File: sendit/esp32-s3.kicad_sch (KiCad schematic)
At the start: 47 parts, among them J9 USB_TYPE_C_16PIN, Q1 FDC6330L, Q2 S8050, Q3 S8050, SW1 RESET, SW2 BOOT, U1 ESP32-S3-WROOM-1-N16R8, U2 USBLC6-2SC6, U3 XC6210B332MR, U4 CH334F, U5 CH343P, Y1 12Mhz, Y2 32.768kHz

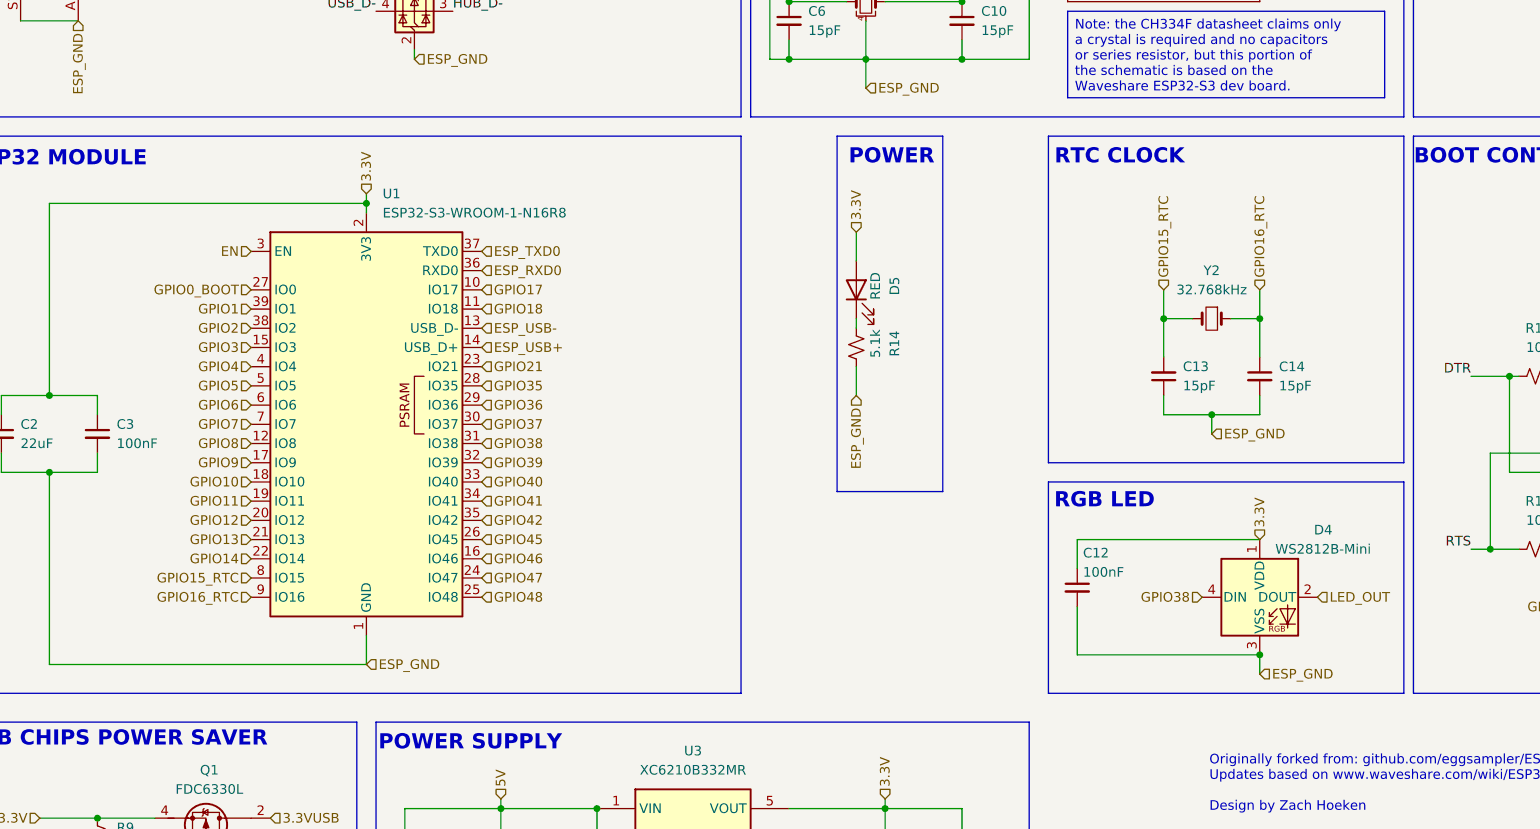
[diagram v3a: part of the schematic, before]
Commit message: started work on the rev c schematic
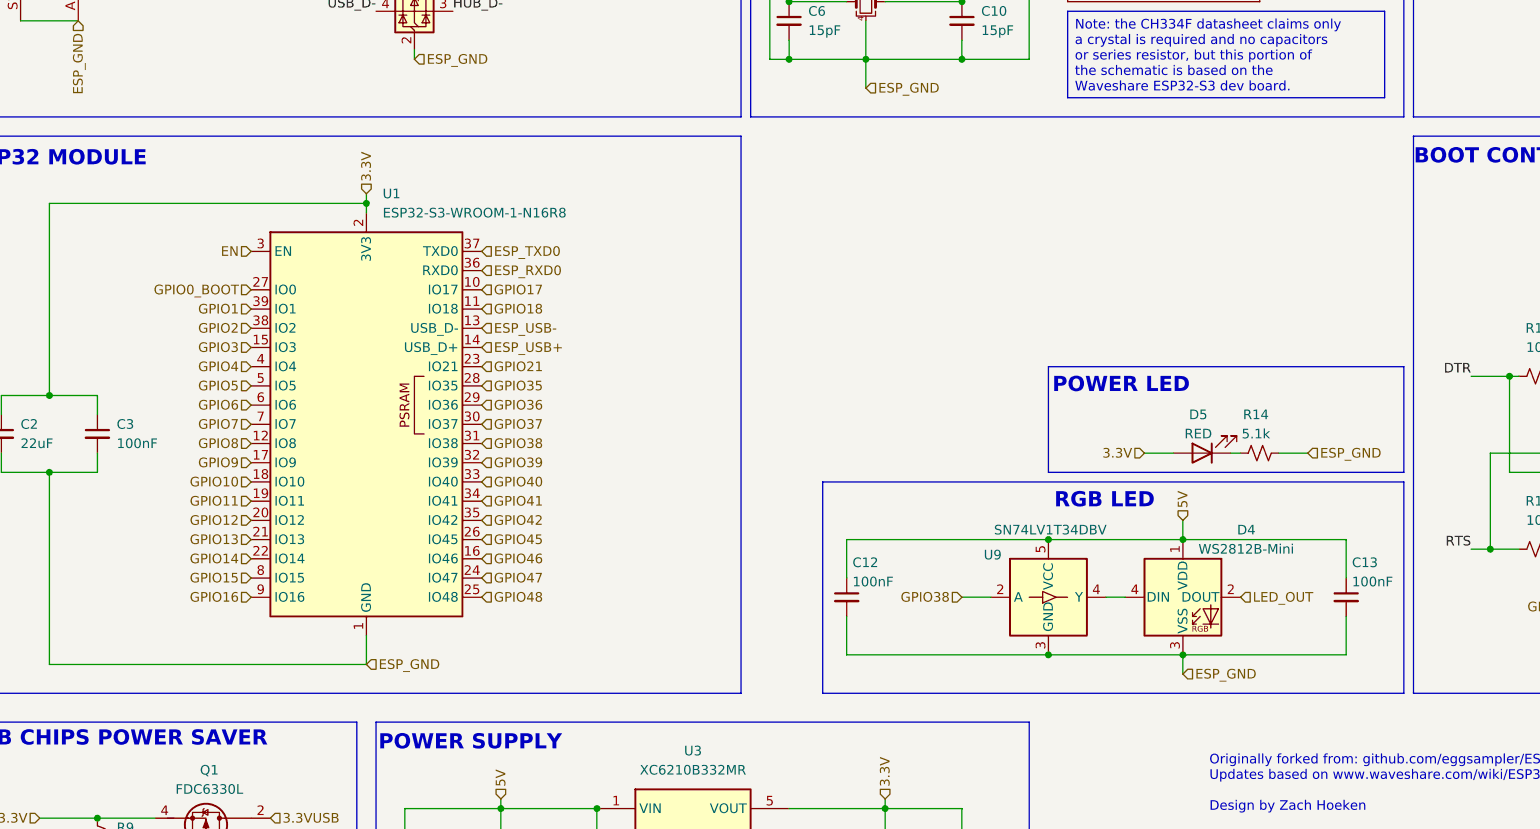
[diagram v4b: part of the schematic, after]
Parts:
- removed C14: 15pF, Capacitor_SMD:C_0603_1608Metric, symbol Device:C_Small
- removed Y2: 32.768kHz, Crystal:Crystal_SMD_3215-2Pin_3.2x1.5mm, symbol Device:Crystal_Small
- added U9: SN74LV1T34DBV, Package_TO_SOT_SMD:SOT-23-5, symbol Logic_LevelTranslator:SN74LV1T34DBV
- C13: value 15pF -> 100nF
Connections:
- net 3.3V: no longer C12.1, D4.1 (VDD)
- net 5V: now also C12.1, C13.1, D4.1 (VDD), U9.5 (VCC)
- net ESP_GND: now also C13.2, U9.3 (GND); no longer C13.1
- net GPIO38: now also U9.2 (A); no longer D4.4 (DIN)
- net GPIO15_RTC renamed GPIO15
- net GPIO15: no longer C13.2
- net GPIO16_RTC renamed GPIO16
- new net: D4.4 (DIN), U9.4 (Y)
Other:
- note added: "POWER LED"
- note removed: "POWER"
- note removed: "RTC CLOCK"
- moved on the sheet: C12, D4, D5, R14

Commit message: more work on rev c board schematic
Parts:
- added TP20: ~, TestPoint:TestPoint_THTPad_D2.0mm_Drill1.0mm, symbol Connector:TestPoint
- D5: value RED -> GREEN
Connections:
- net 3.3V: now also TP20.1
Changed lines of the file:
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@@
 	)
 	(junction
+		(at 72.39 175.26)
+		(diameter 0)
+		(color 0 0 0 0)
+	)
+	(junction
 		(at 31.75 176.53)
 		(diameter 0)
@@
 	)
 	(junction
+		(at 146.05 175.26)
+		(diameter 0)
+		(color 0 0 0 0)
+	)
+	(junction
 		(at 229.87 35.56)
 		(diameter 0)
@@
 	(wire
 		(pts
-			(xy 85.09 173.99) (xy 85.09 175.26)
+			(xy 72.39 173.99) (xy 72.39 175.26)
 		)
 		(stroke
@@
 	(wire
 		(pts
+			(xy 72.39 175.26) (xy 85.09 175.26)
+		)
+		(stroke
+			(width 0)
+			(type default)
+		)
+	)
+	(wire
+		(pts
 			(xy 144.78 26.67) (xy 144.78 27.94)
 		)
@@
 	(wire
 		(pts
-			(xy 135.89 173.99) (xy 135.89 175.26)
+			(xy 146.05 173.99) (xy 146.05 175.26)
 		)
 		(stroke
@@
 	(wire
 		(pts
-			(xy 85.09 175.26) (xy 72.39 175.26)
-		)
-		(stroke
-			(width 0)
-			(type default)
-		)
-	)
-	(wire
-		(pts
 			(xy 218.44 45.72) (xy 228.6 45.72)
 		)
@@
 	(hierarchical_label "5V"
 		(shape input)
-		(at 85.09 173.99 90)
+		(at 72.39 173.99 90)
 		(effects
 			(font
@@
 	(hierarchical_label "3.3V"
 		(shape input)
-		(at 135.89 173.99 90)
+		(at 146.05 173.99 90)
 		(effects
 			(font
@@
 			)
 		)
-		(property "Value" "RED"
+		(property "Value" "GREEN"
 			(at 177.292 125.73 0)
 			(effects
@@
 					(unit 1)
 				)
+			)
+		)
+	)
+	(symbol
+		(lib_id "Connector:TestPoint")
+		(at 135.89 175.26 0)
+		(unit 1)
+		(exclude_from_sim no)
+		(in_bom no)
+		(on_board yes)
+		(dnp no)
+		(property "Reference" "TP20"
+			(at 134.366 170.18 0)
+			(effects
+				(font
+					(size 1.27 1.27)
+				)
+				(justify left)
+			)
+		)
+		(property "Value" "~"
+			(at 138.43 173.2279 0)
+			(effects
+				(font
+					(size 1.27 1.27)
+				)
+				(justify left)
+				(hide yes)
+			)
+		)
+		(property "Footprint" "TestPoint:TestPoint_THTPad_D2.0mm_Drill1.0mm"
+			(at 140.97 175.26 0)
+			(effects
+				(font
+					(size 1.27 1.27)
+				)
+				(hide yes)
+			)
+		)
+		(property "Datasheet" "~"
+			(at 140.97 175.26 0)
+			(effects
+				(font
+					(size 1.27 1.27)
+				)
+				(hide yes)
+			)
+		)
+		(property "Description" "test point"
+			(at 135.89 175.26 0)
+			(effects
+				(font
+					(size 1.27 1.27)
+				)
+				(hide yes)
+			)
+		)
+		(property "LCSC Part Name" ""
+			(at 135.89 175.26 0)
+			(effects
+				(font
+					(size 1.27 1.27)
+				)
+				(hide yes)
+			)
+		)
+		(property "Manufacturer" ""
+			(at 135.89 175.26 0)
+			(effects
+				(font
+					(size 1.27 1.27)
+				)
+				(hide yes)
+			)
+		)
+		(property "Manufacturer Part" ""
+			(at 135.89 175.26 0)
+			(effects
+				(font
+					(size 1.27 1.27)
+				)
+				(hide yes)
+			)
+		)
+		(property "Supplier" ""
+			(at 135.89 175.26 0)
+			(effects
+				(font
+					(size 1.27 1.27)
+				)
+				(hide yes)
+			)
+		)
+		(property "Supplier Part" ""
+			(at 135.89 175.26 0)
+			(effects
+				(font
+					(size 1.27 1.27)
+				)
+				(hide yes)
+			)
+		)
+		(pin "1"
+		)
+		(instances
+			(project "sendit"
+				(path "/a355e4d0-2918-44fc-be8d-2503b84c6d6c/2c30bc70-ed79-4c81-9563-e6b5b53d9914"
+					(reference "TP20")
+					(unit 1)
+				)

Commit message: most of the work on the schematic is done.
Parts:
- renumbered C9 to C10, C10 to C11, C11 to C12, C15 to C14, C16 to C15, C17 to C16, C18 to C17, C19 to C18, C20 to C19, C12 to C7, C7 to C8, C8 to C9, TP20 to TP5, U9 to U4, U4 to U5, U5 to U6
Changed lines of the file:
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@@
 		(dnp no)
 		(fields_autoplaced yes)
-		(property "Reference" "U4"
+		(property "Reference" "U5"
 			(at 172.72 16.51 0)
 			(effects
@@
 			(project "sendit"
 				(path "/a355e4d0-2918-44fc-be8d-2503b84c6d6c/2c30bc70-ed79-4c81-9563-e6b5b53d9914"
-					(reference "U4")
+					(reference "U5")
 					(unit 1)
 				)
@@
 		(on_board yes)
 		(dnp no)
-		(property "Reference" "TP20"
+		(property "Reference" "TP5"
 			(at 134.366 170.18 0)
 			(effects
@@
 			(project "sendit"
 				(path "/a355e4d0-2918-44fc-be8d-2503b84c6d6c/2c30bc70-ed79-4c81-9563-e6b5b53d9914"
-					(reference "TP20")
+					(reference "TP5")
 					(unit 1)
 				)
@@
 		(on_board yes)
 		(dnp no)
-		(property "Reference" "C10"
+		(property "Reference" "C11"
 			(at 148.59 69.8562 0)
 			(effects
@@
 			(project "sendit"
 				(path "/a355e4d0-2918-44fc-be8d-2503b84c6d6c/2c30bc70-ed79-4c81-9563-e6b5b53d9914"
-					(reference "C10")
+					(reference "C11")
 					(unit 1)
 				)
@@
 		(on_board yes)
 		(dnp no)
-		(property "Reference" "U9"
+		(property "Reference" "U4"
 			(at 150.114 141.732 0)
 			(effects
@@
 			(project ""
 				(path "/a355e4d0-2918-44fc-be8d-2503b84c6d6c/2c30bc70-ed79-4c81-9563-e6b5b53d9914"
-					(reference "U9")
+					(reference "U4")
 					(unit 1)
 				)
@@
 		(dnp no)
 		(fields_autoplaced yes)
-		(property "Reference" "C16"
+		(property "Reference" "C15"
 			(at 232.41 31.7562 0)
 			(effects
@@
 			(project "sendit"
 				(path "/a355e4d0-2918-44fc-be8d-2503b84c6d6c/2c30bc70-ed79-4c81-9563-e6b5b53d9914"
-					(reference "C16")
+					(reference "C15")
 					(unit 1)
 				)
@@
 		(dnp no)
 		(fields_autoplaced yes)
-		(property "Reference" "C19"
+		(property "Reference" "C18"
 			(at 247.65 116.8462 0)
 			(effects
@@
 			(project "sendit"
 				(path "/a355e4d0-2918-44fc-be8d-2503b84c6d6c/2c30bc70-ed79-4c81-9563-e6b5b53d9914"
-					(reference "C19")
+					(reference "C18")
 					(unit 1)
 				)
@@
 		(on_board yes)
 		(dnp no)
-		(property "Reference" "C7"
+		(property "Reference" "C8"
 			(at 135.8836 20.32 90)
 			(effects
@@
 			(project "sendit"
 				(path "/a355e4d0-2918-44fc-be8d-2503b84c6d6c/2c30bc70-ed79-4c81-9563-e6b5b53d9914"
-					(reference "C7")
+					(reference "C8")
 					(unit 1)
 				)
@@
 		(dnp no)
 		(fields_autoplaced yes)
-		(property "Reference" "U5"
+		(property "Reference" "U6"
 			(at 257.4133 66.04 0)
 			(effects
@@
 			(project "sendit"
 				(path "/a355e4d0-2918-44fc-be8d-2503b84c6d6c/2c30bc70-ed79-4c81-9563-e6b5b53d9914"
-					(reference "U5")
+					(reference "U6")
 					(unit 1)
 				)
@@
 		(dnp no)
 		(fields_autoplaced yes)
-		(property "Reference" "C20"
+		(property "Reference" "C19"
 			(at 247.65 135.8962 0)
 			(effects
@@
 			(project "sendit"
 				(path "/a355e4d0-2918-44fc-be8d-2503b84c6d6c/2c30bc70-ed79-4c81-9563-e6b5b53d9914"
-					(reference "C20")
+					(reference "C19")
 					(unit 1)
 				)
@@
 		(on_board yes)
 		(dnp no)
-		(property "Reference" "C8"
+		(property "Reference" "C9"
 			(at 135.89 35.306 90)
 			(effects
@@
 			(project "sendit"
 				(path "/a355e4d0-2918-44fc-be8d-2503b84c6d6c/2c30bc70-ed79-4c81-9563-e6b5b53d9914"
-					(reference "C8")
+					(reference "C9")
 					(unit 1)
 				)
@@
 		(on_board yes)
 		(dnp no)
-		(property "Reference" "C15"
+		(property "Reference" "C14"
 			(at 220.98 31.7562 0)
 			(effects
@@
 			(project "sendit"
 				(path "/a355e4d0-2918-44fc-be8d-2503b84c6d6c/2c30bc70-ed79-4c81-9563-e6b5b53d9914"
-					(reference "C15")
+					(reference "C14")
 					(unit 1)
 				)
@@
 		(dnp no)
 		(fields_autoplaced yes)
-		(property "Reference" "C18"
+		(property "Reference" "C17"
 			(at 243.84 31.7562 0)
 			(effects
@@
 			(project "sendit"
 				(path "/a355e4d0-2918-44fc-be8d-2503b84c6d6c/2c30bc70-ed79-4c81-9563-e6b5b53d9914"
-					(reference "C18")
+					(reference "C17")
 					(unit 1)
 				)
@@
 		(dnp no)
 		(fields_autoplaced yes)
-		(property "Reference" "C11"
+		(property "Reference" "C12"
 			(at 148.59 180.3462 0)
 			(effects
@@
 			(project "sendit"
 				(path "/a355e4d0-2918-44fc-be8d-2503b84c6d6c/2c30bc70-ed79-4c81-9563-e6b5b53d9914"
-					(reference "C11")
+					(reference "C12")
 					(unit 1)
 				)
@@
 		(on_board yes)
 		(dnp no)
-		(property "Reference" "C12"
+		(property "Reference" "C7"
 			(at 131.572 142.748 0)
 			(effects
@@
 			(project "sendit"
 				(path "/a355e4d0-2918-44fc-be8d-2503b84c6d6c/2c30bc70-ed79-4c81-9563-e6b5b53d9914"
-					(reference "C12")
+					(reference "C7")
 					(unit 1)
 				)
@@
 		(dnp no)
 		(fields_autoplaced yes)
-		(property "Reference" "C17"
+		(property "Reference" "C16"
 			(at 231.1463 39.37 90)
 			(effects
@@
 			(project "sendit"
 				(path "/a355e4d0-2918-44fc-be8d-2503b84c6d6c/2c30bc70-ed79-4c81-9563-e6b5b53d9914"
-					(reference "C17")
+					(reference "C16")
 					(unit 1)
 				)
@@
 		(dnp no)
 		(fields_autoplaced yes)
-		(property "Reference" "C9"
+		(property "Reference" "C10"
 			(at 138.43 180.3462 0)
 			(effects
@@
 			(project "sendit"
 				(path "/a355e4d0-2918-44fc-be8d-2503b84c6d6c/2c30bc70-ed79-4c81-9563-e6b5b53d9914"
-					(reference "C9")
+					(reference "C10")
 					(unit 1)
 				)

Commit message: more work towards rev c board.
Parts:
- SW1, SW2: footprint Button_Switch_THT:SW_Tactile_SPST_Angled_PTS645Vx58-2LFS -> Button_Switch_SMD:SW_SPST_B3U-1000P; LCSC C557599 -> C231329; Rotation Offset 180 -> (none)
- TP5: footprint TestPoint:TestPoint_THTPad_D2.0mm_Drill1.0mm -> TestPoint:TestPoint_THTPad_D1.5mm_Drill0.7mm
- renumbered J9 to J8, R8 to R10, R9 to R11, R10 to R12, R11 to R13, R12 to R14, R13 to R15, R14 to R16, R15 to R17, R16 to R18, R17 to R19, R18 to R20
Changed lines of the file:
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@@
 		(on_board yes)
 		(dnp no)
-		(property "Reference" "R12"
+		(property "Reference" "R14"
 			(at 57.15 43.18 90)
 			(effects
@@
 			(project "sendit"
 				(path "/a355e4d0-2918-44fc-be8d-2503b84c6d6c/2c30bc70-ed79-4c81-9563-e6b5b53d9914"
-					(reference "R12")
+					(reference "R14")
 					(unit 1)
 				)
@@
 		(on_board yes)
 		(dnp no)
-		(property "Reference" "R14"
+		(property "Reference" "R16"
 			(at 184.912 123.19 90)
 			(effects
@@
 			(project "sendit"
 				(path "/a355e4d0-2918-44fc-be8d-2503b84c6d6c/2c30bc70-ed79-4c81-9563-e6b5b53d9914"
-					(reference "R14")
+					(reference "R16")
 					(unit 1)
 				)
@@
 			)
 		)
-		(property "Footprint" "TestPoint:TestPoint_THTPad_D2.0mm_Drill1.0mm"
+		(property "Footprint" "TestPoint:TestPoint_THTPad_D1.5mm_Drill0.7mm"
 			(at 140.97 175.26 0)
 			(effects
@@
 		(dnp no)
 		(fields_autoplaced yes)
-		(property "Reference" "R15"
+		(property "Reference" "R17"
 			(at 222.25 111.76 90)
 			(effects
@@
 			(project "sendit"
 				(path "/a355e4d0-2918-44fc-be8d-2503b84c6d6c/2c30bc70-ed79-4c81-9563-e6b5b53d9914"
-					(reference "R15")
+					(reference "R17")
 					(unit 1)
 				)
@@
 		(dnp no)
 		(fields_autoplaced yes)
-		(property "Reference" "R8"
+		(property "Reference" "R10"
 			(at 25.4 180.34 90)
 			(effects
@@
 			(project "sendit"
 				(path "/a355e4d0-2918-44fc-be8d-2503b84c6d6c/2c30bc70-ed79-4c81-9563-e6b5b53d9914"
-					(reference "R8")
+					(reference "R10")
 					(unit 1)
 				)
@@
 		(dnp no)
 		(fields_autoplaced yes)
-		(property "Reference" "R16"
+		(property "Reference" "R18"
 			(at 222.25 134.62 90)
 			(effects
@@
 			(project "sendit"
 				(path "/a355e4d0-2918-44fc-be8d-2503b84c6d6c/2c30bc70-ed79-4c81-9563-e6b5b53d9914"
-					(reference "R16")
+					(reference "R18")
 					(unit 1)
 				)
@@
 			)
 		)
-		(property "Footprint" "Button_Switch_THT:SW_Tactile_SPST_Angled_PTS645Vx58-2LFS"
+		(property "Footprint" "Button_Switch_SMD:SW_SPST_B3U-1000P"
 			(at 269.24 105.41 0)
 			(effects
@@
 			)
 		)
-		(property "LCSC" "C557599"
-			(at 269.24 110.49 0)
-			(effects
-				(font
-					(size 1.27 1.27)
-				)
-				(hide yes)
-			)
-		)
-		(property "Rotation Offset" "180"
+		(property "LCSC" "C231329"
 			(at 269.24 110.49 0)
 			(effects
@@
 		(on_board yes)
 		(dnp no)
-		(property "Reference" "R13"
+		(property "Reference" "R15"
 			(at 143.51 66.04 90)
 			(effects
@@
 			(project "sendit"
 				(path "/a355e4d0-2918-44fc-be8d-2503b84c6d6c/2c30bc70-ed79-4c81-9563-e6b5b53d9914"
-					(reference "R13")
+					(reference "R15")
 					(unit 1)
 				)
@@
 		(dnp no)
 		(fields_autoplaced yes)
-		(property "Reference" "R10"
+		(property "Reference" "R12"
 			(at 34.29 187.9599 0)
 			(effects
@@
 			(project "sendit"
 				(path "/a355e4d0-2918-44fc-be8d-2503b84c6d6c/2c30bc70-ed79-4c81-9563-e6b5b53d9914"
-					(reference "R10")
+					(reference "R12")
 					(unit 1)
 				)
@@
 			)
 		)
-		(property "Footprint" "Button_Switch_THT:SW_Tactile_SPST_Angled_PTS645Vx58-2LFS"
+		(property "Footprint" "Button_Switch_SMD:SW_SPST_B3U-1000P"
 			(at 269.24 143.51 0)
 			(effects
@@
 			)
 		)
-		(property "LCSC" "C557599"
-			(at 269.24 148.59 0)
-			(effects
-				(font
-					(size 1.27 1.27)
-				)
-				(hide yes)
-			)
-		)
-		(property "Rotation Offset" "180"
+		(property "LCSC" "C231329"
 			(at 269.24 148.59 0)
 			(effects
@@
 		(dnp no)
 		(fields_autoplaced yes)
-		(property "Reference" "J9"
+		(property "Reference" "J8"
 			(at 29.21 25.4 0)
 			(effects
@@
 			(project "sendit"
 				(path "/a355e4d0-2918-44fc-be8d-2503b84c6d6c/2c30bc70-ed79-4c81-9563-e6b5b53d9914"
-					(reference "J9")
+					(reference "J8")
 					(unit 1)
 				)
@@
 		(dnp no)
 		(fields_autoplaced yes)
-		(property "Reference" "R18"
+		(property "Reference" "R20"
 			(at 259.08 142.2399 0)
 			(effects
@@
 			(project "sendit"
 				(path "/a355e4d0-2918-44fc-be8d-2503b84c6d6c/2c30bc70-ed79-4c81-9563-e6b5b53d9914"
-					(reference "R18")
+					(reference "R20")
 					(unit 1)
 				)
@@
 		(on_board yes)
 		(dnp no)
-		(property "Reference" "R11"
+		(property "Reference" "R13"
 			(at 57.15 35.56 90)
 			(effects
@@
 			(project "sendit"
 				(path "/a355e4d0-2918-44fc-be8d-2503b84c6d6c/2c30bc70-ed79-4c81-9563-e6b5b53d9914"
-					(reference "R11")
+					(reference "R13")
 					(unit 1)
 				)
@@
 		(dnp no)
 		(fields_autoplaced yes)
-		(property "Reference" "R9"
+		(property "Reference" "R11"
 			(at 34.29 177.7999 0)
 			(effects
@@
 			(project "sendit"
 				(path "/a355e4d0-2918-44fc-be8d-2503b84c6d6c/2c30bc70-ed79-4c81-9563-e6b5b53d9914"
-					(reference "R9")
+					(reference "R11")
 					(unit 1)
 				)
@@
 		(dnp no)
 		(fields_autoplaced yes)
-		(property "Reference" "R17"
+		(property "Reference" "R19"
 			(at 259.08 105.4099 0)
 			(effects
@@
 			(project "sendit"
 				(path "/a355e4d0-2918-44fc-be8d-2503b84c6d6c/2c30bc70-ed79-4c81-9563-e6b5b53d9914"
-					(reference "R17")
+					(reference "R19")
 					(unit 1)
 				)

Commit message: power system work and layout
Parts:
- renumbered J8 to J9
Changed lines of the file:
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@@
 		(dnp no)
 		(fields_autoplaced yes)
-		(property "Reference" "J8"
+		(property "Reference" "J9"
 			(at 29.21 25.4 0)
 			(effects
@@
 			(project "sendit"
 				(path "/a355e4d0-2918-44fc-be8d-2503b84c6d6c/2c30bc70-ed79-4c81-9563-e6b5b53d9914"
-					(reference "J8")
+					(reference "J9")
 					(unit 1)
 				)
